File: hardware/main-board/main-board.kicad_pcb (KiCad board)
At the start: 2 copper layers, 48 x 48 mm, 44 parts, among them J1 USB-C Receptacle, J2 JST JWPF, J3 LCD_FFC_SOLDER, Q1 SS8050-G, Q2 SS8050-G, Q3 SS8050-G, SW1 FRONT_BUTTON, U1 SN65HVD230, U2 CPC1017N, U3 AP1509-33SG-13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

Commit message: updated LCD to proper board footprint, added additional 3d models
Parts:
- SW1: footprint Button_Switch_SMD:SW_SPST_B3S-1100 -> main-board-custom-footprints:SW_SPST_B3S-1100
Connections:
- U5 pad 39: GND -> (no net)

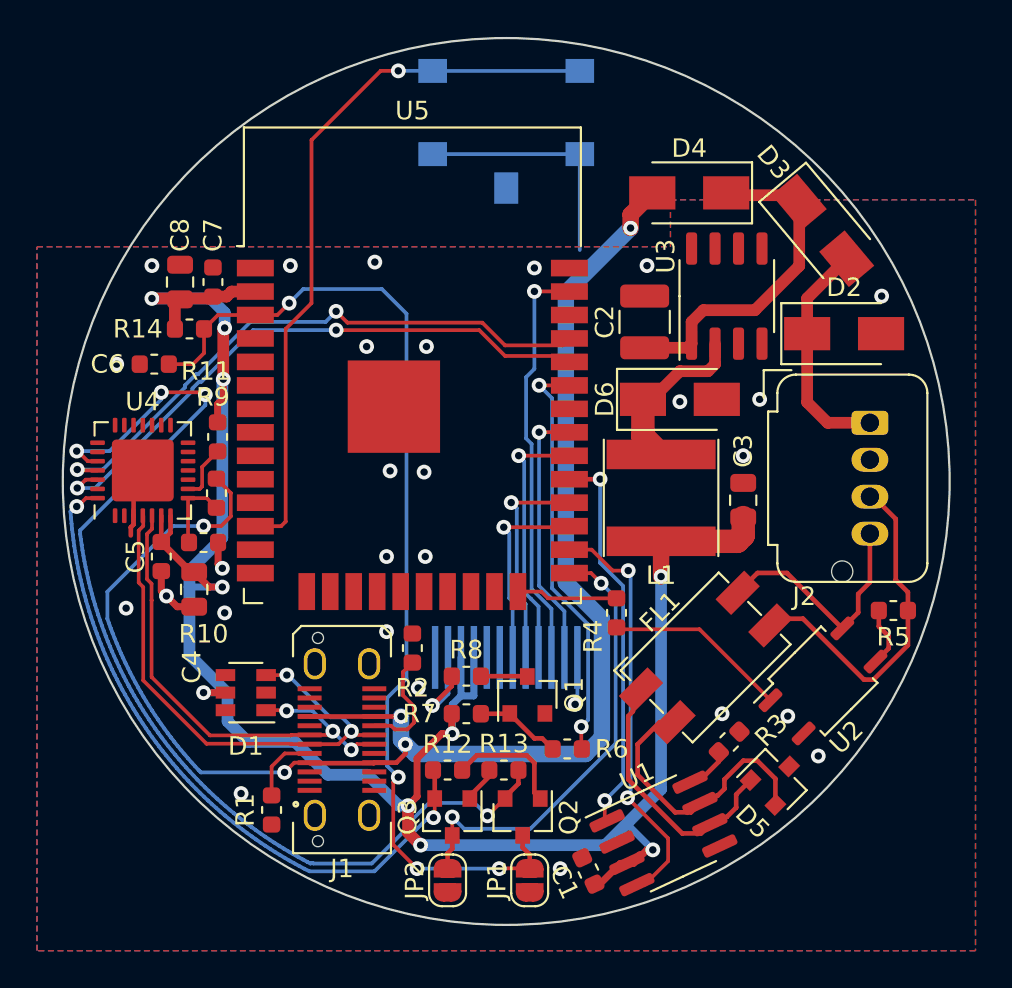
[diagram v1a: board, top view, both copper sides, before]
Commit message: added qr code, switched button to a different button. put on reddit for review
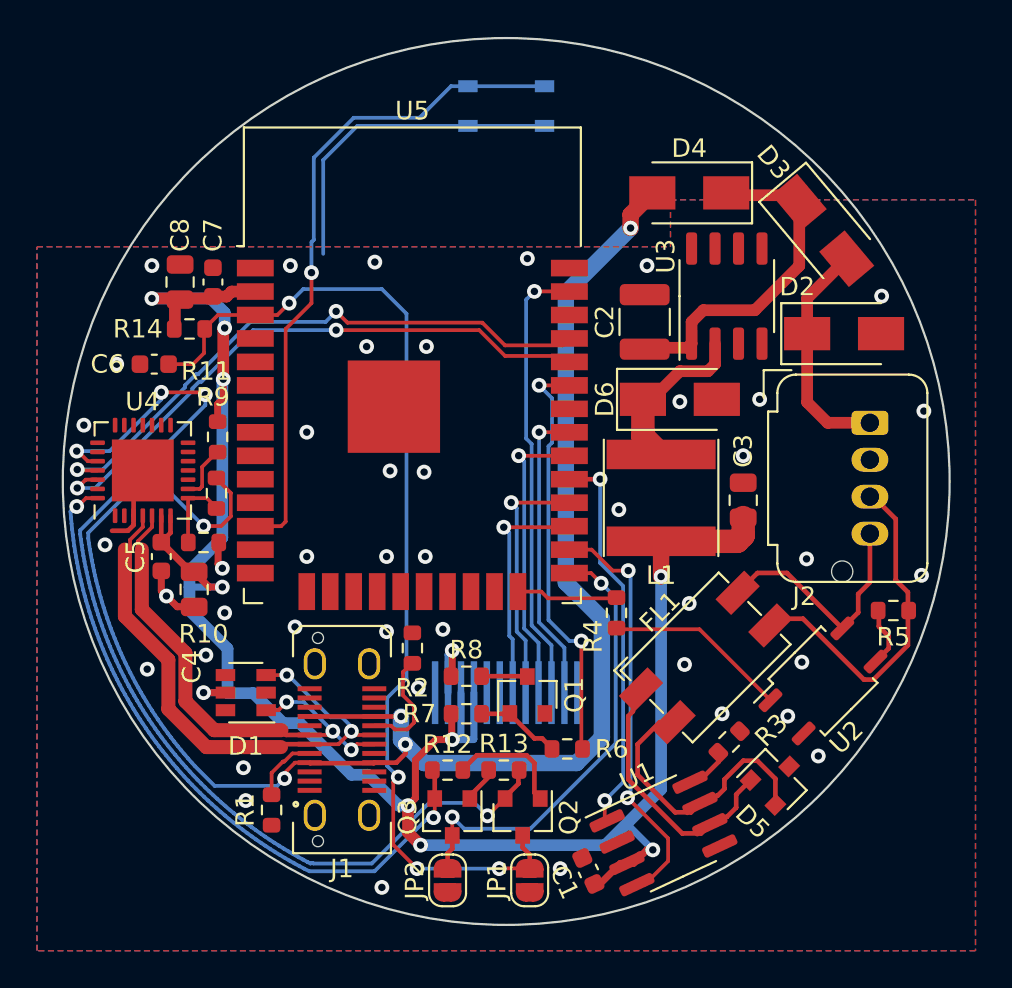
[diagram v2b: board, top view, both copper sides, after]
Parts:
- added G1: LOGO, main-board-custom-footprints:gcan-gauge-github-link-qr, B.Cu at (-6.60, -2.03)
- FL1: value EMI_Filter_CommonMode -> DR331-513AE
- SW1: footprint main-board-custom-footprints:SW_SPST_B3S-1100 -> main-board-custom-footprints:SW_SPST_PTS810
- moved J3 1.90 mm to (0.00, 11.4)
- moved SW1 1.27 mm to (0.00, -20.3)
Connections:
- U5 pad 39: (no net) -> GND
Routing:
- net /USB_VBUS: track 84.0 -> 89.7 mm
- net /ESP32/FRONT_BUTTON: track 39.0 -> 36.2 mm
- net GND: track 24.2 -> 27.0 mm, vias 28 -> 43
- net /ESP32/LCD_SCL: track 14.1 -> 16.0 mm
- net /LCD/DC: track 10.8 -> 12.7 mm
- net /ESP32/LCD_RESET: track 14.4 -> 16.3 mm
- net /LCD/CS: track 11.9 -> 13.8 mm
- net /ESP32/LCD_SDO: track 22.5 -> 24.4 mm
- net /USB_D+: track 29.5 -> 30.9 mm
- net Net-(J3-Pad2): track 5.10 -> 3.79 mm
- net /USB_D-: track 27.0 -> 28.2 mm
- net +3V3: track 117.3 -> 116.2 mm
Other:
- net class USB added: clearance 0.1524, trace_width 0.762, via_dia 0.8, via_drill 0.4
- board text added: "For 1.28in IPS LCD 52mm enclosure"
- board text added: "Programmable Digital CANbus Gauge WHillier 21.213"
- board text added: "gCAN Gauge"
- board text added: "github.com/willemcvu/gCAN-gauge"

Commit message: Added mounting holes, tweaked layout to accomodate.
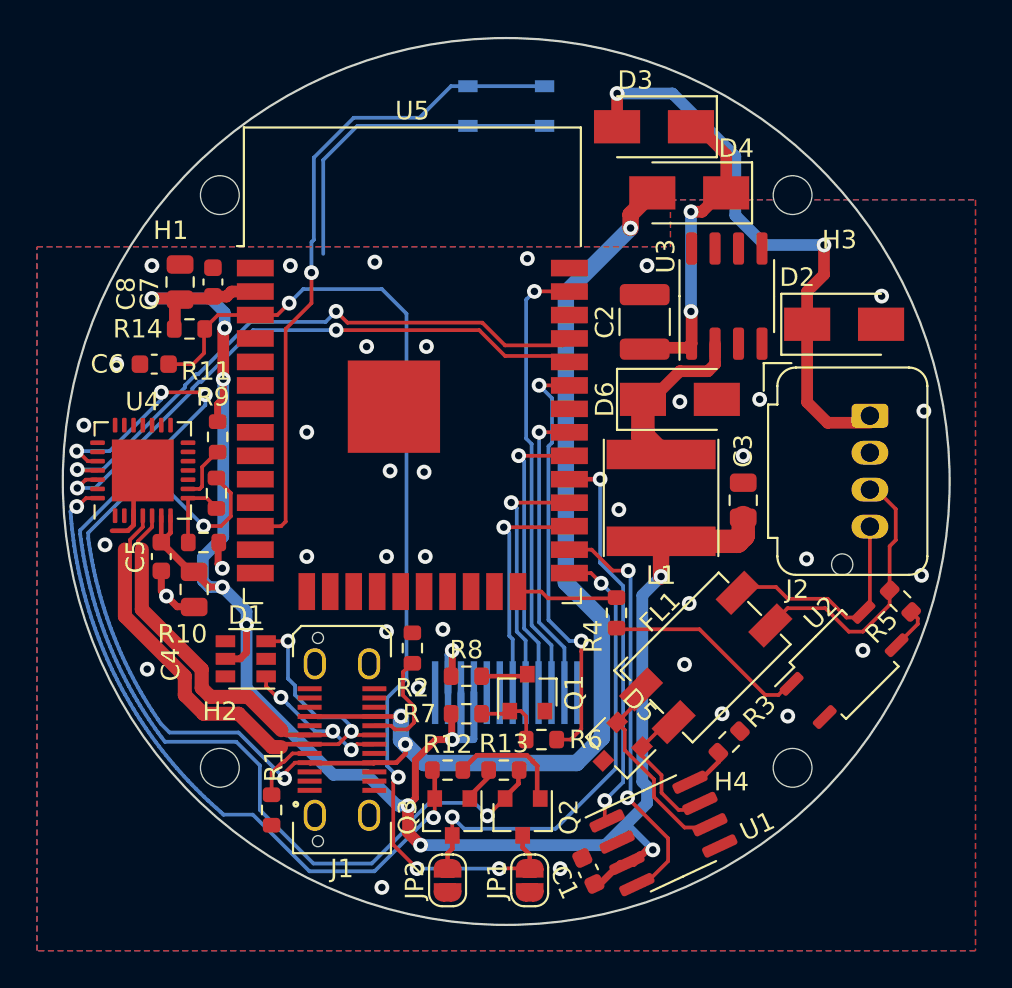
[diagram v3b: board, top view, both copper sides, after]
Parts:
- added H1: M2, MountingHole:MountingHole_2.1mm, F.Cu at (-15.5, -15.5)
- added H2: M2, MountingHole:MountingHole_2.1mm, F.Cu at (-15.5, 15.5)
- added H3: M2, MountingHole:MountingHole_2.1mm, F.Cu at (15.5, -15.5)
- added H4: M2, MountingHole:MountingHole_2.1mm, F.Cu at (15.5, 15.5)
- moved D3 10.7 mm to (8.00, -19.2), turned to 180 degrees
- moved D5 8.80 mm to (5.97, 14.4), turned to 225 degrees
- moved D1 1.83 mm to (-14.1, 9.60)
- moved R6 1.49 mm to (1.91, 14.0)
- moved U2 1.45 mm to (18.3, 9.91)
- moved R5 0.64 mm to (21.3, 6.48), turned to 315 degrees
- moved D2 0.51 mm to (18.3, -8.51)
- moved J2 0.38 mm to (19.7, -3.56)
- moved Q1 0.13 mm to (1.14, 11.4)
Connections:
- FL1 pad 1: Net-(D5-Pad1) -> Net-(D5-Pad2)
- FL1 pad 2: Net-(D5-Pad2) -> Net-(D5-Pad1)
- U1 pad 6: Net-(D5-Pad1) -> Net-(D5-Pad2)
- U1 pad 7: Net-(D5-Pad2) -> Net-(D5-Pad1)
- U5 pad 39: GND -> (no net)
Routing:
- net /12V_IN: track 12.5 -> 31.0 mm, vias 0 -> 2
- net Net-(D5-Pad1): track 14.6 -> 7.79 mm
- net Net-(D5-Pad2): track 15.7 -> 11.0 mm
- net /CANH: track 18.7 -> 15.1 mm
- net +3V3: track 116.2 -> 113.9 mm
- net /VBUS: track 18.5 -> 16.7 mm, vias 0 -> 2
- net /ESP32/~RTS: track 57.5 -> 59.1 mm
- net Net-(R4-Pad1): track 9.97 -> 11.2 mm
- net Net-(R5-Pad2): track 3.28 -> 2.42 mm
- net Net-(Q1-Pad1): track 4.70 -> 3.87 mm
- net /USB_D+: track 30.9 -> 31.7 mm
- net /ESP32/IO0: track 24.8 -> 25.6 mm
- net /USB_D-: track 28.2 -> 27.6 mm
- net /CANL: track 13.1 -> 12.5 mm
- net GND: vias 43 -> 37

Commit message: exported gerbers. Shipping 21.218.
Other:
- board text added: "Programmable Digital CANbus Gauge WHillier 21.218"
- board text removed: "Programmable Digital CANbus Gauge WHillier 21.213"
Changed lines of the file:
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@@
   )
   (setup
-    (last_trace_width 0.2032)
+    (last_trace_width 0.25)
     (user_trace_width 0.2032)
     (user_trace_width 0.254)
@@
       (outputformat 1)
       (mirror false)
-      (drillshape 1)
+      (drillshape 0)
       (scaleselection 1)
-      (outputdirectory ""))
+      (outputdirectory "gerbers/"))
   )
   (net 0 "")
@@
     (effects (font (size 0.75 0.75) (thickness 0.14)) (justify left mirror))
   )
-  (gr_text "Programmable Digital CANbus Gauge\nWHillier  21.213" (at 13.843 -12.954) (layer B.SilkS)
+  (gr_text "Programmable Digital CANbus Gauge\nWHillier  21.218" (at 13.843 -12.954) (layer B.SilkS)
     (effects (font (size 1 1) (thickness 0.15)) (justify left mirror))
   )
